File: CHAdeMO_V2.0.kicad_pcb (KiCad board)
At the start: 4 copper layers, 100 x 107.7 mm, 131 parts, among them IC1 ISO1050DUBR, IC2 ISO1050DUBR, J1 UJ2-BV-1-TH, J2 5810132011, J3 39-28-8020, J4 B2B-PH-K-S(LF)(SN), K1 V23086C1001A403-EV-BLBOX, Q1 IRLML0060TRPBF, Q2 IRLML0060TRPBF, Q3 IRLML0060TRPBF, Q4 IRLML0060TRPBF, Q5 DMP4065SQ-7, U1 M24M02-DRMN6TP, U2 ATSAM3X8EA-AU, U3 VOM617A-4T, U4 VOM617A-4T, U5 VOM617A-4T, U6 VOM617A-4T, U7 VOM617A-4T, Y1 CRYSTAL 12MHZ, Y2 Crystal 32.768kHz

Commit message: Ordered 2.0.2 22/12 at JLCPCB
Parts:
- moved R3 4.65 mm to (89.7, 102.5)
- moved L2 4.29 mm to (82.2, 112.8)
- moved C26 4.24 mm to (82.3, 108.6)
- moved C25 4.19 mm to (82.3, 110.9)
- moved R18 3.36 mm to (102.7, 141.2), turned to 90 degrees
- moved R17 2.91 mm to (104.9, 141.2)
- moved R14 2.59 mm to (85.3, 81.9)
- moved C15 1.91 mm to (94.2, 141.9)
- moved C6 1.91 mm to (91.7, 141.9)
- moved C9 1.91 mm to (96.5, 141.9)
- moved C1 1.78 mm to (80.6, 135.4)
- moved C22 1.78 mm to (80.6, 130.6)
- moved C14 1.56 mm to (113.1, 128.7)
- moved C17 1.56 mm to (113.1, 131.1)
- moved C24 1.48 mm to (107.3, 110.1), turned to 0 degrees
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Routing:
- net /VDD_OUT: track 101.0 -> 108.7 mm
- net +3V3: track 98.9 -> 106.4 mm
- net Net-(R3-Pad1): track 12.8 -> 18.6 mm
- net +12V: track 107.8 -> 112.2 mm
- net /CHAdeMO-charge-start1_3.3Vsignal_IN1_D6: track 73.6 -> 77.4 mm
- net /VDD_ANA: track 6.41 -> 9.97 mm
- net /CHAdeMO-CHARGE-START2_IN2: track 38.9 -> 42.1 mm
- net /CHAdeMO_contactor2-feedback_D11: track 74.7 -> 77.7 mm
- net /CHAdeMO_contactor1-feedback_D27: track 76.8 -> 79.3 mm
- net /CHAdeMO-charge-start2_3.3Vsignal_IN2_D7: track 60.5 -> 62.9 mm
- net /CAN0-TX: track 40.0 -> 42.4 mm
- net /CAN0-RX: track 42.4 -> 44.7 mm
- net /Relay_CHAdeMO_contactors_GND: track 8.74 -> 10.5 mm
- net /CHAdeMO-charge-enable-signal_D48: track 72.4 -> 74.0 mm
- net /VDD_PLL: track 7.15 -> 8.69 mm
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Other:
- board text added: "CHAdeMO Controller v2.0.2 Lars Rengersen 2021"
- board text removed: "CHAdeMO Controller v2.0.1 Lars Rengersen 2020"

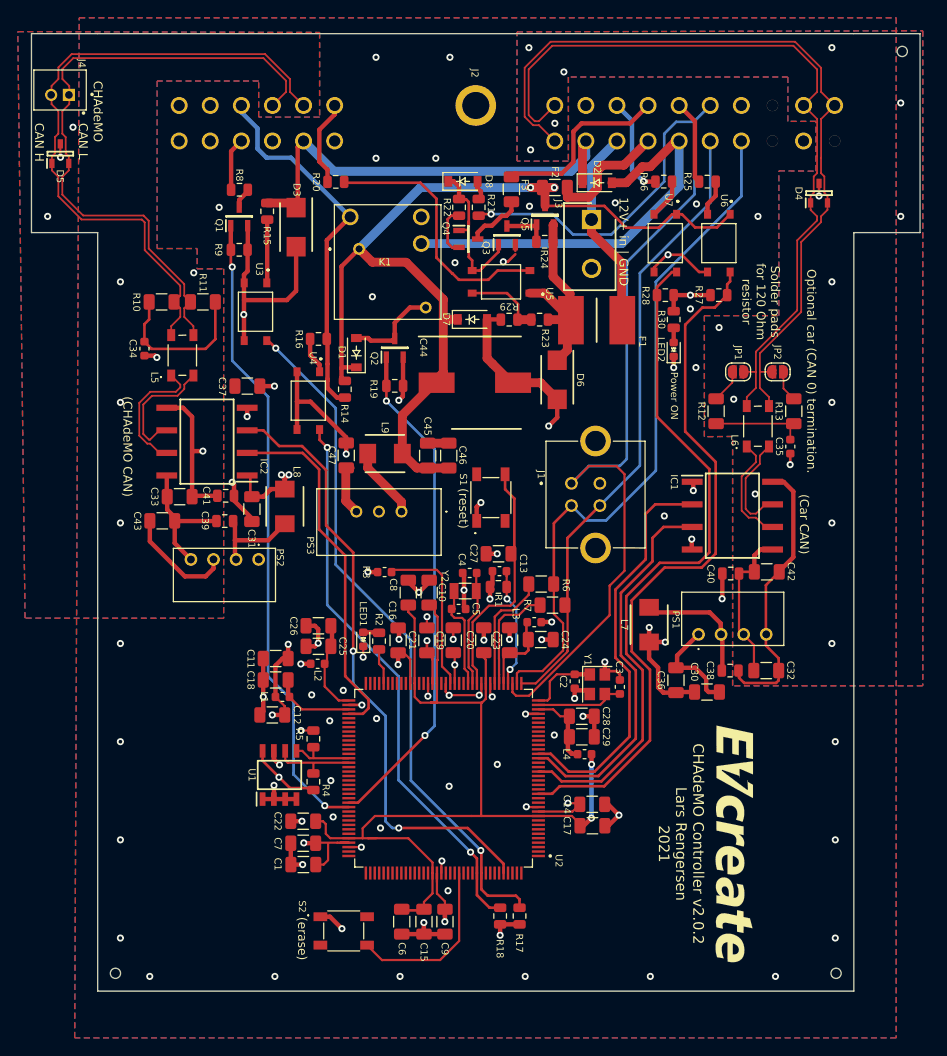
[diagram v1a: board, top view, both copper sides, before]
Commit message: Dummy footprints
For stencil with cutouts for JLCPCB placed components
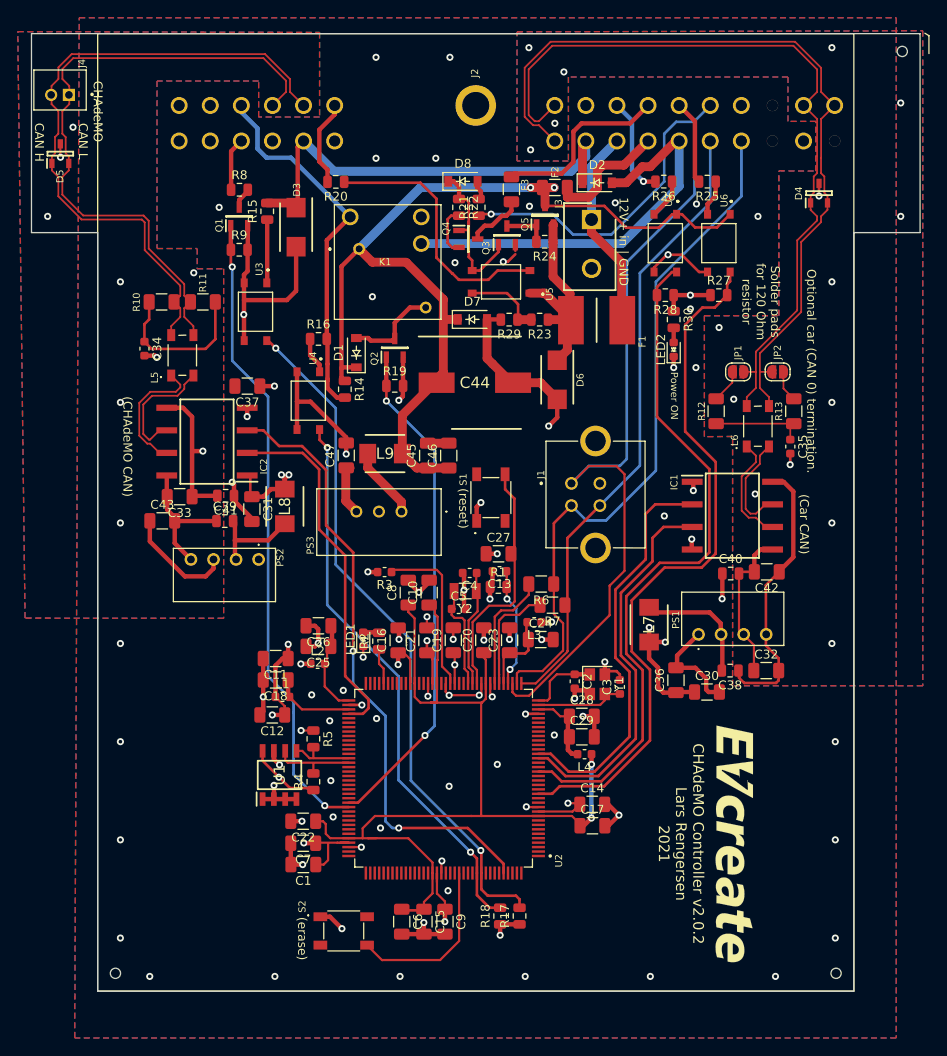
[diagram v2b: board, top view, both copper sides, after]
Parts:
- C1, C10, C11, C12, C14, C15, C16, C17, C18, C19, C20, C21, C22, C23, C24, C25, C26, C27, C28, C29, C30, C31, C32, C33, C36, C37, C42, C43, C45, C46, C47, C6, C7, C8, C9: footprint Capacitor_SMD:C_1206_3216Metric -> Components:DummyC1206_C_1206_3216Metric
- C13, C2, C3, C34, C35, C4, C5: footprint Capacitor_SMD:C_0603_1608Metric -> Components:Dummy_C_0603_1608Metric
- C38, C39, C40, C41: footprint Capacitor_SMD:C_0805_2012Metric -> Components:Dummy_C0805_210x135
- C44: footprint SamacSys_Parts:CAPAE1040X1050N -> Components:Dummy_ECAP_CAPAE1040X1050N
- D1, D2, D7, D8: footprint Diode_SMD:D_SOD-123 -> Components:Dummy_D_SOD-123
- L1, L2, L3, L4: footprint Inductor_SMD:L_0603_1608Metric -> Components:Dummy_L_0603_1608Metric
- L7, L8, L9: footprint Components:INDPM4442X200N -> Components:Dummy_L420_INDPM4442X200N
- LED1, LED2: footprint LED_SMD:LED_0603_1608Metric -> Components:Dummy_LED_0603_1608Metric
- R1, R14, R15, R16, R17, R18, R19, R2, R20, R21, R22, R23, R24, R25, R26, R27, R28, R29, R30, R4, R5, R8, R9: footprint Resistor_SMD:R_0805_2012Metric -> Components:Dummy_R_0805_2012Metric
- R3: footprint Resistor_SMD:R_0603_1608Metric -> Components:Dummy_R_0603_1608Metric
- R6, R7: footprint Resistor_SMD:R_1206_3216Metric -> Components:Dummy_R_1206_3216Metric
- U1: footprint SamacSys_Parts:SOIC127P600X175-8N -> Components:Dummy_SOIC8_SOIC127P600X175-8N
- Y1: footprint Crystal:Crystal_SMD_3225-4Pin_3.2x2.5mm -> Components:Dummy_Crystal_SMD_3225-4Pin_3.2x2.5mm
- Y2: footprint Crystal:Crystal_SMD_3215-2Pin_3.2x1.5mm -> Components:Dummy_Crystal_SMD_3215-2Pin_3.2x1.5mm
